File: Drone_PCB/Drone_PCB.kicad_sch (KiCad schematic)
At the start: 29 parts, among them J1 Conn_01x04_Pin, J2 Conn_01x04_Pin, J3 Conn_01x04_Pin, J4 Conn_01x06_Pin, J5 Conn_01x06_Pin, U1 STM32F411RCT6, U2 AP2112K-3.3, Y1 26MHz

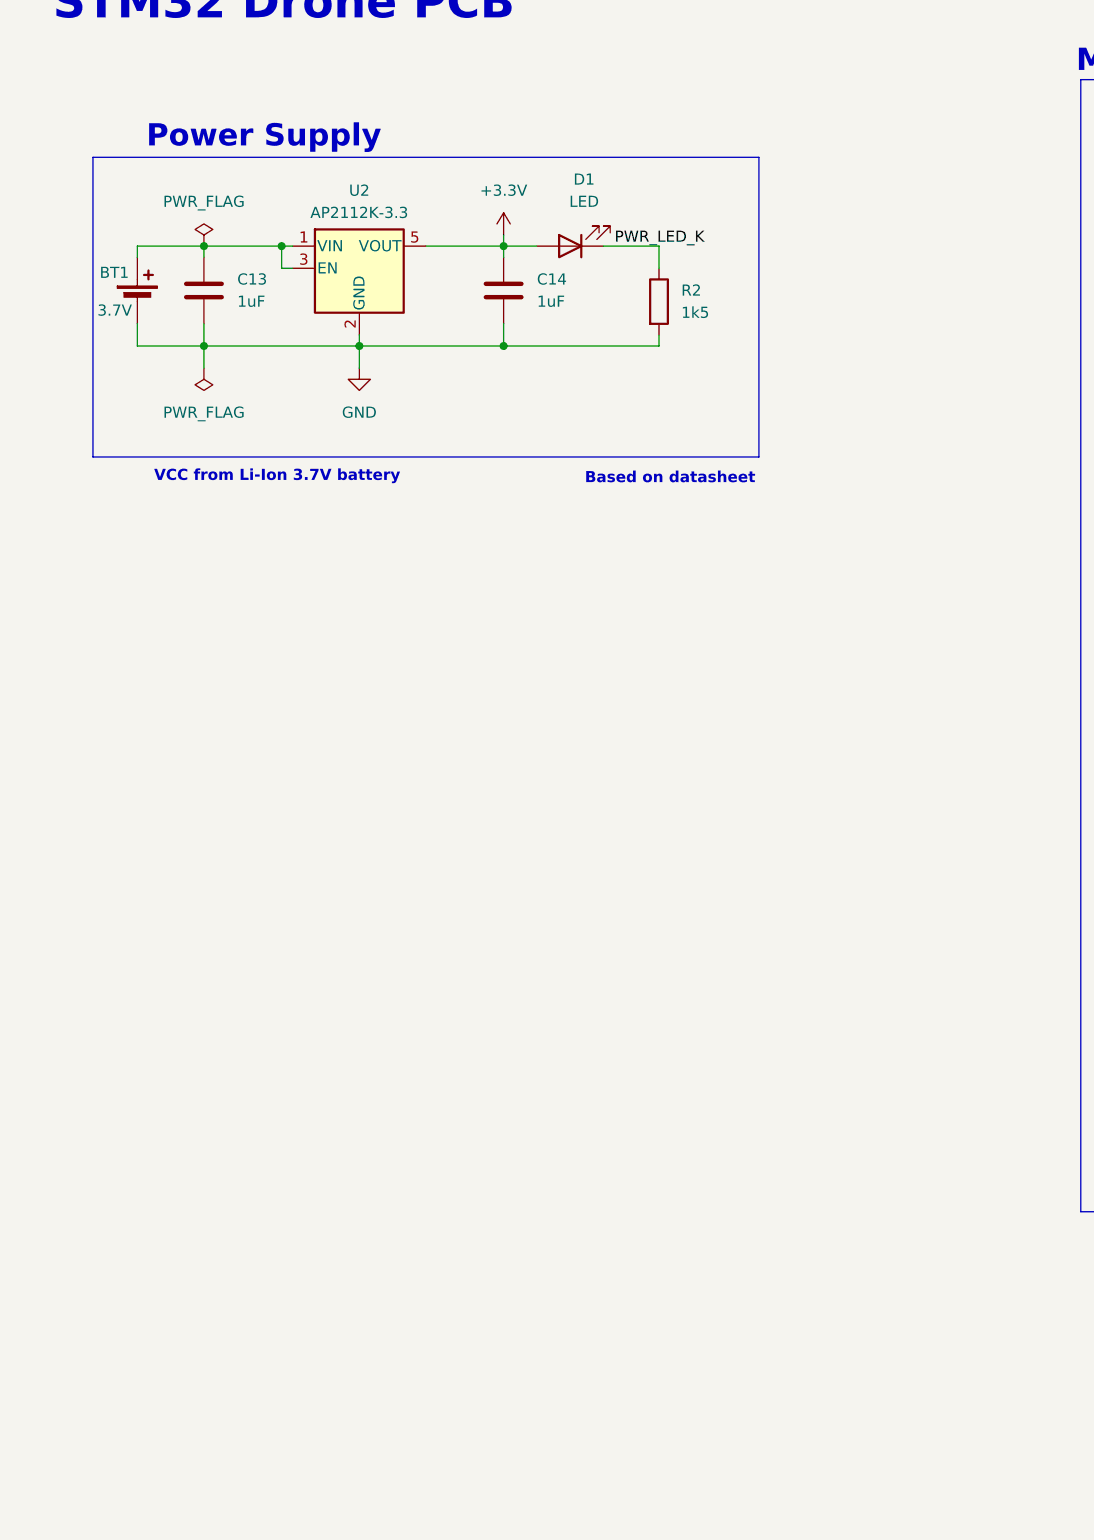
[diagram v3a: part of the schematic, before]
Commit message: Added charging module
FIX THAT connections are wrong 4some reason
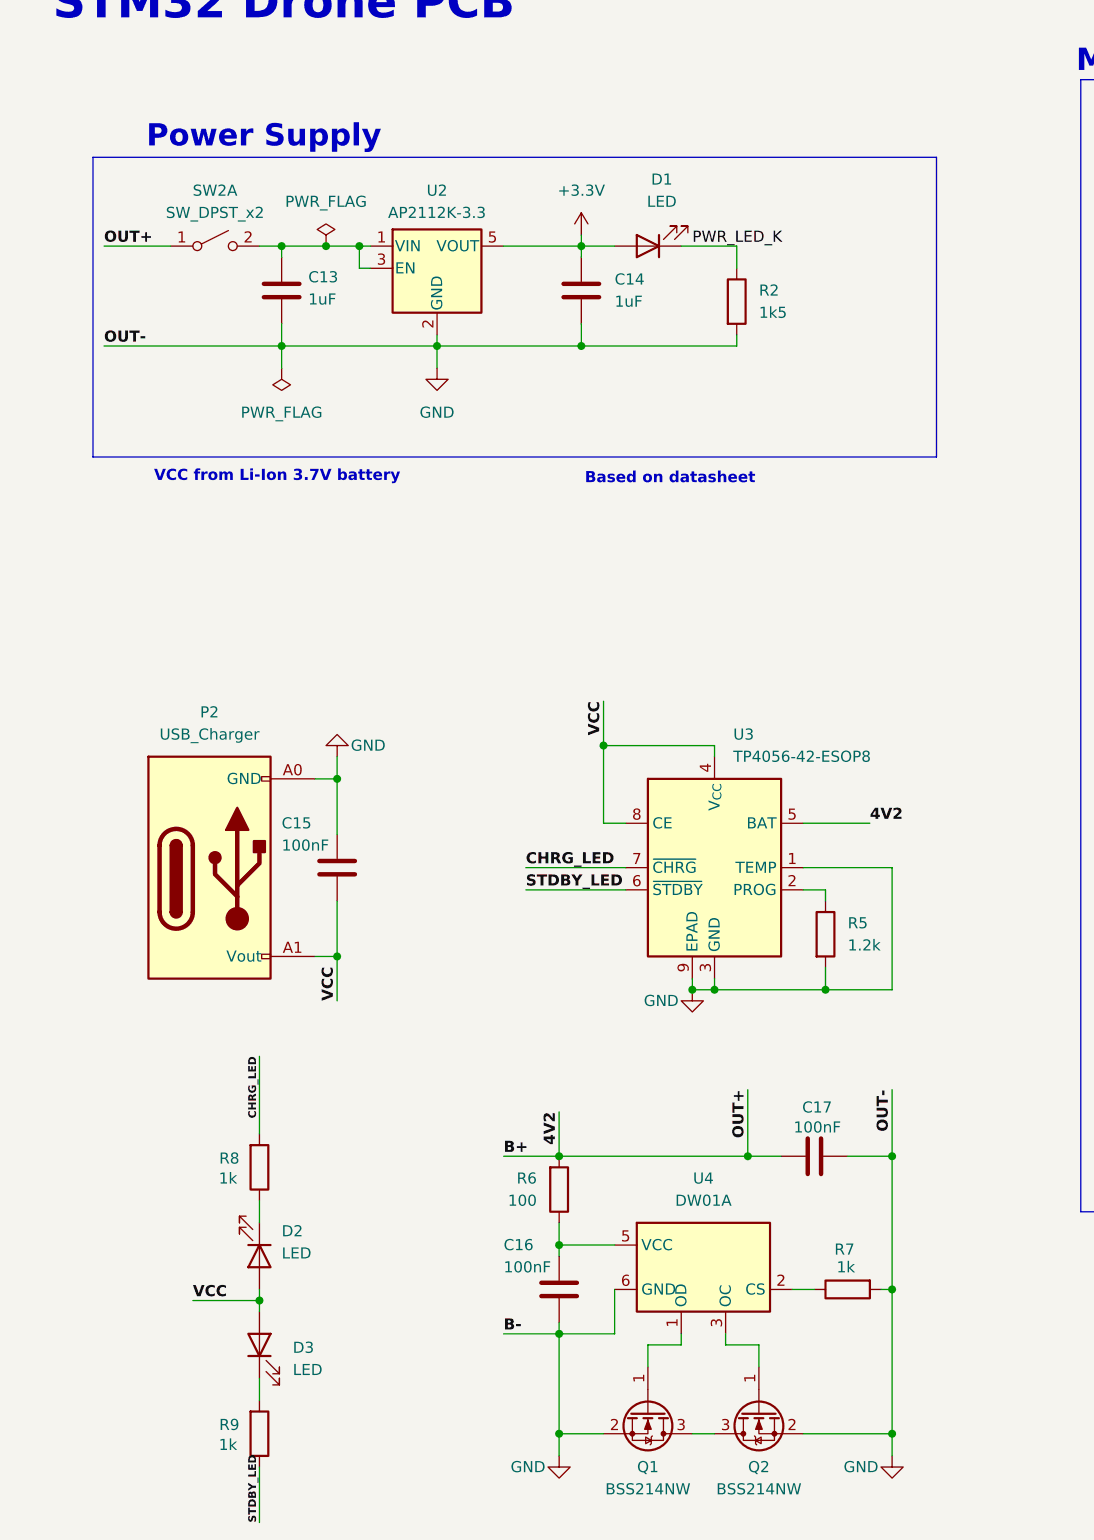
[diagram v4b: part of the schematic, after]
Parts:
- removed BT1: 3.7V, symbol Device:Battery_Cell
- added C15, C16, C17: 100nF, symbol Device:C
- added D2, D3: LED, symbol Device:LED
- added P2: USB_Charger, symbol MyLibrary:USB_Charger
- added Q1, Q2: BSS214NW, Package_TO_SOT_SMD:SOT-323_SC-70, symbol Transistor_FET:BSS214NW
- added R5: 1.2k, symbol Device:R
- added R6: 100, symbol Device:R
- added R7, R8, R9: 1k, symbol Device:R
- added SW2: SW_DPST_x2, symbol Switch:SW_DPST_x2
- added U3: TP4056-42-ESOP8, Package_SO:SOIC-8-1EP_3.9x4.9mm_P1.27mm_EP2.41x3.3mm_ThermalVias, symbol Battery_Management:TP4056-42-ESOP8
- added U4: DW01A, Package_TO_SOT_SMD:SOT-23-6, symbol Battery_Management:DW01A
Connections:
- net GND: now also C15.1, C16.2, C17.2, P2.A0 (GND), Q1.2 (S), Q2.2 (S), R5.2, R7.2, U3.1 (TEMP), U3.3 (GND), U3.9 (EPAD), U4.6 (GND)
- net at C13.1, U2.1 (VIN), U2.3 (EN): now also SW2.2 (B)
- new net: C16.1, R6.1, U4.5 (VCC)
- new net: Q1.1 (G), U4.1 (OD)
- new net: Q1.3 (D), Q2.3 (D)
- new net: R7.1, U4.2 (CS)
- new net: D3.1 (K), R9.2
- new net: Q2.1 (G), U4.3 (OC)
- new net: D2.1 (K), R8.1
- new net: R5.1, U3.2 (PROG)
- new net 4V2: C17.1, R6.2, SW2.1 (A), U3.5 (BAT)
- new net CHRG_LED: R8.2, U3.7 (~{CHRG})
- new net STDBY_LED: R9.1, U3.6 (~{STDBY})
- new net VCC: C15.2, D2.2 (A), D3.2 (A), P2.A1 (Vout), U3.4 (V_{CC}), U3.8 (CE)
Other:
- moved on the sheet: C13, C14, D1, R2, U2

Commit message: Fixed errors
Now everything looks good
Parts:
- removed P2: USB_Charger, symbol MyLibrary:USB_Charger
- added J6: USB_B_Micro, symbol Connector:USB_B_Micro
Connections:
- net 4V2 is gone; now on net VCC: C17.1, R6.2, SW2.1 (A), U3.5 (BAT)
- net GND: now also J6.5 (GND), J6.6 (Shield)
- net VCC: no longer C15.2, U3.4 (V_{CC}), U3.8 (CE)
- new net VBUS: C15.2, J6.1 (VBUS), U3.4 (V_{CC}), U3.8 (CE)
- no-connect marks 38 -> 41
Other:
- moved on the sheet: C15, C16, C17, D2, D3, Q1, Q2, R5, R6, R7, R8, R9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

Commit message: Footprint assignment
We assigned footprints
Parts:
- C1, C10, C11, C12, C2, C3, C4, C5, C7, C8, C9: footprint (none) -> Capacitor_SMD:C_0402_1005Metric
- C13, C14: value 1uF -> 1u; footprint (none) -> Capacitor_SMD:C_0402_1005Metric
- C15, C16, C17: value 100nF -> 100n; footprint (none) -> Capacitor_SMD:C_0402_1005Metric
- C6: footprint (none) -> Capacitor_SMD:C_0603_1608Metric
- D1: value LED -> BLUE_LED; footprint (none) -> LED_SMD:LED_0603_1608Metric
- D2: value LED -> RED_LED; footprint (none) -> LED_SMD:LED_0603_1608Metric
- D3: value LED -> GREEN_LED; footprint (none) -> LED_SMD:LED_0603_1608Metric
- FB1: footprint (none) -> Inductor_SMD:L_0603_1608Metric
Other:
- note added: "Anti-discharge scheme"
- note added: "Charging Section"
- note added: "Chargning IC"
- note added: "LED indicators"
- note added: "USB B Micro connector"
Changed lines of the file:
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@@
 	)
 	(rectangle
+		(start 17.78 97.79)
+		(end 114.3 195.58)
+		(stroke
+			(width 0)
+			(type default)
+		)
+		(fill
+			(type none)
+		)
+	)
+	(rectangle
 		(start 17.78 35.56)
 		(end 114.3 69.85)
@@
 		)
 	)
+	(text "USB B Micro connector"
+		(exclude_from_sim no)
+		(at 31.496 188.722 0)
+		(effects
+			(font
+				(size 1.27 1.27)
+				(thickness 0.254)
+				(bold yes)
+			)
+		)
+	)
 	(text "Power Supply"
 		(exclude_from_sim no)
@@
 		)
 	)
+	(text "LED indicators"
+		(exclude_from_sim no)
+		(at 34.544 157.48 0)
+		(effects
+			(font
+				(size 1.27 1.27)
+				(thickness 0.254)
+				(bold yes)
+			)
+		)
+	)
+	(text "Chargning IC"
+		(exclude_from_sim no)
+		(at 85.852 140.462 0)
+		(effects
+			(font
+				(size 1.27 1.27)
+				(thickness 0.254)
+				(bold yes)
+			)
+		)
+	)
 	(text "VCC from Li-Ion 3.7V battery"
 		(exclude_from_sim no)
@@
 		)
 	)
+	(text "Anti-discharge scheme"
+		(exclude_from_sim no)
+		(at 79.248 193.548 0)
+		(effects
+			(font
+				(size 1.27 1.27)
+				(thickness 0.254)
+				(bold yes)
+			)
+		)
+	)
 	(text "Microcontroller"
 		(exclude_from_sim no)
@@
 		)
 	)
+	(text "Charging Section"
+		(exclude_from_sim no)
+		(at 36.576 94.742 0)
+		(effects
+			(font
+				(size 2.54 2.54)
+				(thickness 1.27)
+				(bold yes)
+			)
+		)
+	)
 	(text "VDDA Filtering"
 		(exclude_from_sim no)
@@
 			)
 		)
-		(property "Footprint" ""
+		(property "Footprint" "Inductor_SMD:L_0603_1608Metric"
 			(at 247.65 41.148 90)
 			(effects
@@
 			)
 		)
-		(property "Value" "100nF"
+		(property "Value" "100n"
 			(at 93.218 149.098 90)
 			(effects
@@
 			)
 		)
-		(property "Footprint" ""
+		(property "Footprint" "Capacitor_SMD:C_0402_1005Metric"
 			(at 93.98 151.4348 0)
 			(effects
@@
 			)
 		)
-		(property "Footprint" ""
+		(property "Footprint" "Capacitor_SMD:C_0402_1005Metric"
 			(at 258.7752 48.26 0)
 			(effects
@@
 			)
 		)
-		(property "Footprint" ""
+		(property "Footprint" "Capacitor_SMD:C_0402_1005Metric"
 			(at 158.4452 86.36 0)
 			(effects
@@
 			)
 		)
-		(property "Footprint" ""
+		(property "Footprint" "Capacitor_SMD:C_0402_1005Metric"
 			(at 182.5752 86.36 0)
 			(effects
@@
 			)
 		)
-		(property "Footprint" ""
+		(property "Footprint" "Capacitor_SMD:C_0402_1005Metric"
 			(at 195.2752 48.26 0)
 			(effects
@@
 			)
 		)
-		(property "Footprint" ""
+		(property "Footprint" "Capacitor_SMD:C_0603_1608Metric"
 			(at 138.1252 48.26 0)
 			(effects
@@
 			)
 		)
-		(property "Value" "100nF"
+		(property "Value" "100n"
 			(at 38.608 171.196 0)
 			(effects
@@
 			)
 		)
-		(property "Footprint" ""
+		(property "Footprint" "Capacitor_SMD:C_0402_1005Metric"
 			(at 46.6852 170.18 0)
 			(effects
@@
 			)
 		)
-		(property "Value" "LED"
+		(property "Value" "RED_LED"
 			(at 38.1 124.1424 90)
 			(effects
@@
 			)
 		)
-		(property "Footprint" ""
+		(property "Footprint" "LED_SMD:LED_0603_1608Metric"
 			(at 35.56 124.46 0)
 			(effects
@@
 			)
 		)
-		(property "Footprint" ""
+		(property "Footprint" "Capacitor_SMD:C_0402_1005Metric"
 			(at 160.9852 48.26 0)
 			(effects
@@
 			)
 		)
-		(property "Footprint" ""
+		(property "Footprint" "Capacitor_SMD:C_0402_1005Metric"
 			(at 237.1852 48.26 0)
 			(effects
@@
 			)
 		)
-		(property "Footprint" ""
+		(property "Footprint" "Capacitor_SMD:C_0402_1005Metric"
 			(at 155.9052 67.31 0)
 			(effects
@@
 		)
 		(property "Value" "+3.3VA"
-			(at 216.916 34.036 0)
+			(at 216.408 34.544 0)
 			(effects
 				(font
@@
 			)
 		)
-		(property "Value" "100nF"
+		(property "Value" "100n"
 			(at 54.61 165.1 0)
 			(effects
@@
 			)
 		)
-		(property "Footprint" ""
+		(property "Footprint" "Capacitor_SMD:C_0402_1005Metric"
 			(at 61.9252 171.45 0)
 			(effects
@@
 			)
 		)
-		(property "Footprint" ""
+		(property "Footprint" "Capacitor_SMD:C_0402_1005Metric"
 			(at 225.7552 48.26 0)
 			(effects
@@
 			)
 		)
-		(property "Footprint" ""
+		(property "Footprint" "Capacitor_SMD:C_0402_1005Metric"
 			(at 149.5552 48.26 0)
 			(effects
@@
 			)
 		)
-		(property "Footprint" ""
+		(property "Footprint" "Capacitor_SMD:C_0402_1005Metric"
 			(at 183.8452 48.26 0)
 			(effects
@@
 			)
 		)
-		(property "Value" "LED"
+		(property "Value" "GREEN_LED"
 			(at 39.37 137.4774 90)
 			(effects
@@
 			)
 		)
-		(property "Footprint" ""
+		(property "Footprint" "LED_SMD:LED_0603_1608Metric"
 			(at 35.56 134.62 0)
 			(effects
@@
 			)
 		)
-		(property "Value" "LED"
+		(property "Value" "BLUE_LED"
 			(at 82.8675 40.64 0)
 			(effects
@@
 			)
 		)
-		(property "Footprint" ""
+		(property "Footprint" "LED_SMD:LED_0603_1608Metric"
 			(at 81.28 45.72 0)
 			(effects
@@
 			)
 		)
-		(property "Footprint" ""
+		(property "Footprint" "Capacitor_SMD:C_0402_1005Metric"
 			(at 172.4152 48.26 0)
 			(effects
@@
 			)
 		)
-		(property "Value" "1uF"
+		(property "Value" "1u"
 			(at 42.418 51.816 0)
 			(effects
@@
 			)
 		)
-		(property "Footprint" ""
+		(property "Footprint" "Capacitor_SMD:C_0402_1005Metric"
 			(at 40.3352 54.61 0)
 			(effects
@@
 			)
 		)
-		(property "Value" "1uF"
+		(property "Value" "1u"
 			(at 77.47 52.0699 0)
 			(effects
@@
 			)
 		)
-		(property "Footprint" ""
+		(property "Footprint" "Capacitor_SMD:C_0402_1005Metric"
 			(at 74.6252 54.61 0)
 			(effects

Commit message: Updated footprint
There were missing objects
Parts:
- J1, J2, J3: footprint (none) -> Connector_PinHeader_2.54mm:PinHeader_1x04_P2.54mm_Vertical
- J4, J5: footprint (none) -> Connector_PinHeader_2.54mm:PinHeader_1x06_P2.54mm_Vertical
- J6: footprint (none) -> Connector_USB:USB_Micro-B_Wuerth_629105150521
- R1, R2, R3, R4, R5, R6, R7, R8, R9: footprint (none) -> Resistor_SMD:R_0402_1005Metric
- SW2: footprint (none) -> Button_Switch_THT:SW_E-Switch_EG1224_SPDT_Angled
- Y1: footprint (none) -> Crystal:Crystal_SMD_HC49-SD
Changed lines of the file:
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@@
 			)
 		)
-		(property "Footprint" ""
+		(property "Footprint" "Resistor_SMD:R_0402_1005Metric"
 			(at 59.182 156.21 90)
 			(effects
@@
 			)
 		)
-		(property "Footprint" ""
+		(property "Footprint" "Button_Switch_THT:SW_E-Switch_EG1224_SPDT_Angled"
 			(at 31.75 45.72 0)
 			(effects
@@
 			)
 		)
-		(property "Footprint" ""
+		(property "Footprint" "Connector_PinHeader_2.54mm:PinHeader_1x04_P2.54mm_Vertical"
 			(at 260.35 119.38 0)
 			(effects
@@
 			)
 		)
-		(property "Footprint" ""
+		(property "Footprint" "Connector_USB:USB_Micro-B_Wuerth_629105150521"
 			(at 31.75 175.26 0)
 			(effects
@@
 			)
 		)
-		(property "Footprint" ""
+		(property "Footprint" "Resistor_SMD:R_0402_1005Metric"
 			(at 93.98 165.862 90)
 			(effects
@@
 			)
 		)
-		(property "Footprint" ""
+		(property "Footprint" "Crystal:Crystal_SMD_HC49-SD"
 			(at 171.45 76.2 0)
 			(effects
@@
 			)
 		)
-		(property "Footprint" ""
+		(property "Footprint" "Connector_PinHeader_2.54mm:PinHeader_1x04_P2.54mm_Vertical"
 			(at 162.56 99.06 0)
 			(effects
@@
 			)
 		)
-		(property "Footprint" ""
+		(property "Footprint" "Resistor_SMD:R_0402_1005Metric"
 			(at 33.782 144.78 90)
 			(effects
@@
 			)
 		)
-		(property "Footprint" ""
+		(property "Footprint" "Connector_PinHeader_2.54mm:PinHeader_1x06_P2.54mm_Vertical"
 			(at 259.08 71.12 0)
 			(effects
@@
 			)
 		)
-		(property "Footprint" ""
+		(property "Footprint" "Connector_PinHeader_2.54mm:PinHeader_1x06_P2.54mm_Vertical"
 			(at 162.56 118.11 0)
 			(effects
@@
 			)
 		)
-		(property "Footprint" ""
+		(property "Footprint" "Resistor_SMD:R_0402_1005Metric"
 			(at 84.582 132.08 90)
 			(effects
@@
 			)
 		)
-		(property "Footprint" ""
+		(property "Footprint" "Resistor_SMD:R_0402_1005Metric"
 			(at 89.662 52.07 90)
 			(effects
@@
 			)
 		)
-		(property "Footprint" ""
+		(property "Footprint" "Connector_PinHeader_2.54mm:PinHeader_1x04_P2.54mm_Vertical"
 			(at 260.35 93.98 0)
 			(effects
@@
 			)
 		)
-		(property "Footprint" ""
+		(property "Footprint" "Resistor_SMD:R_0402_1005Metric"
 			(at 33.782 114.3 90)
 			(effects
@@
 			)
 		)
-		(property "Footprint" ""
+		(property "Footprint" "Resistor_SMD:R_0402_1005Metric"
 			(at 242.062 109.22 90)
 			(effects
@@
 			)
 		)
-		(property "Footprint" ""
+		(property "Footprint" "Resistor_SMD:R_0402_1005Metric"
 			(at 172.72 65.278 90)
 			(effects
@@
 			)
 		)
-		(property "Footprint" ""
+		(property "Footprint" "Resistor_SMD:R_0402_1005Metric"
 			(at 230.632 109.22 90)
 			(effects
